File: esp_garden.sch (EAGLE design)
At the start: 40 parts, among them IC1 REG1117, T1 DMN6068SE-13, T2 DMN6068SE-13, T3 DMN6068SE-13, T4 DMN6068SE-13, U1 V1, U10 V1, U11 V1, U12 V1, U14 V1, U15 V1, U2 V1, U3 V1, U4 V1, U5 V1, U6 V1, U7 V1, U8 V1, U9 V1

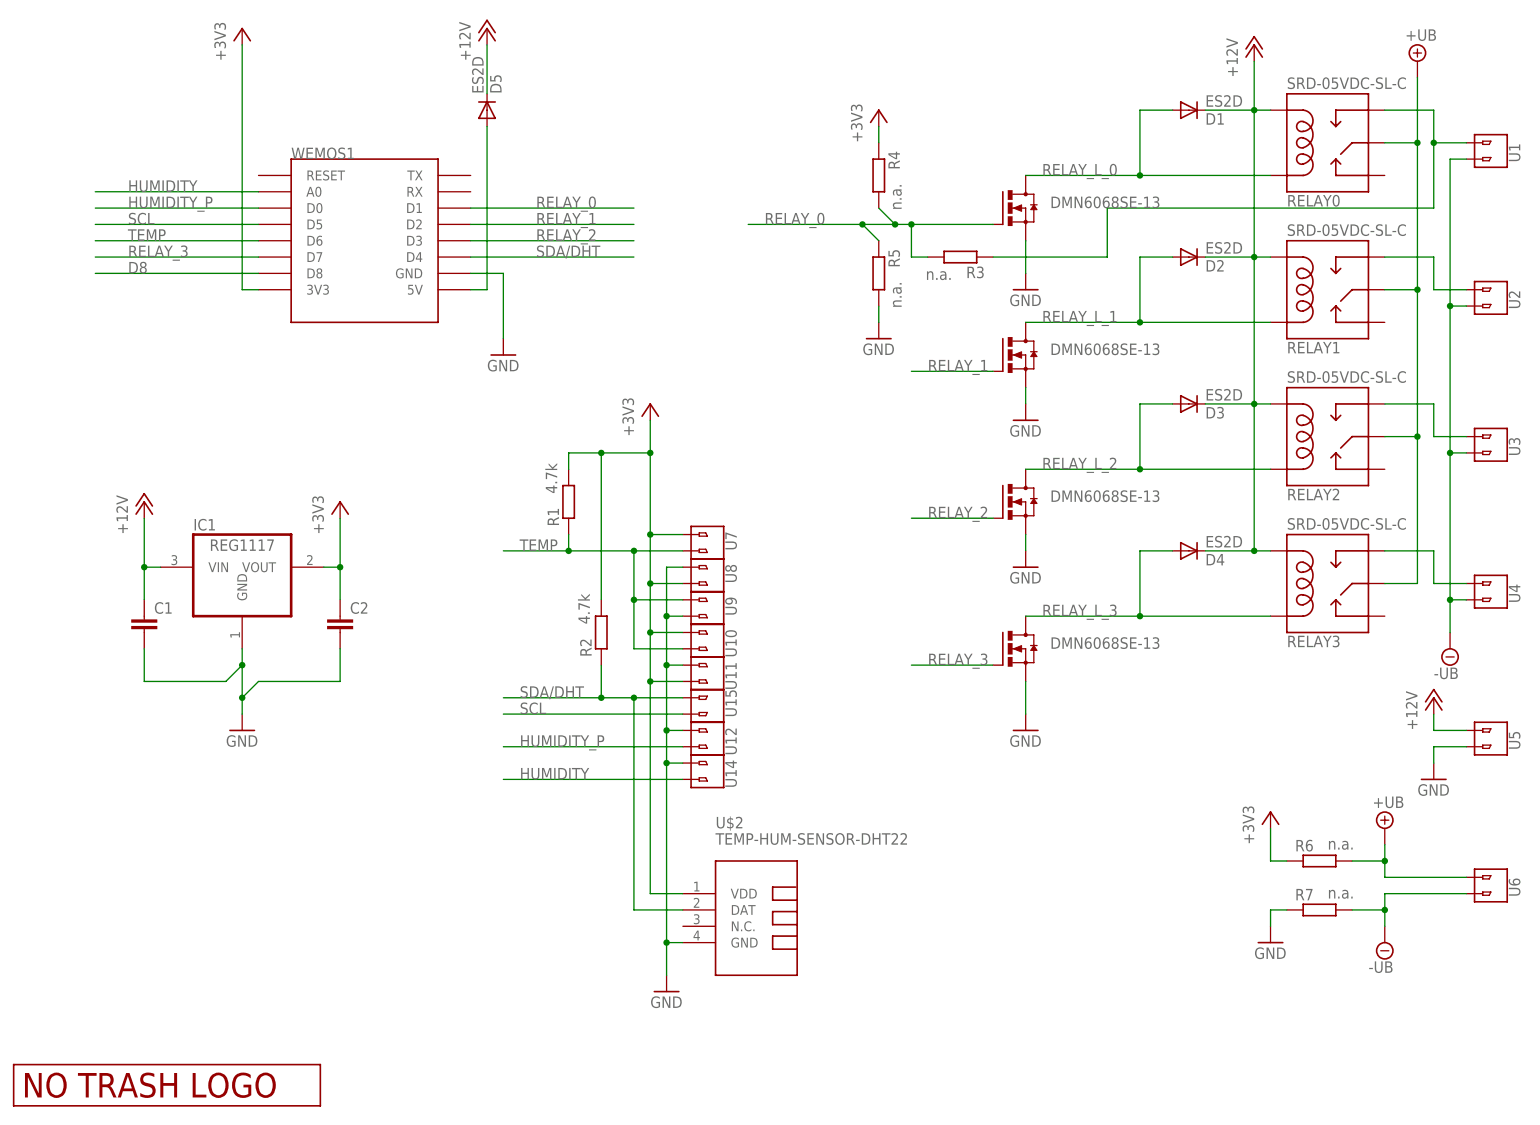
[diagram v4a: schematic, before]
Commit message: added rectifier
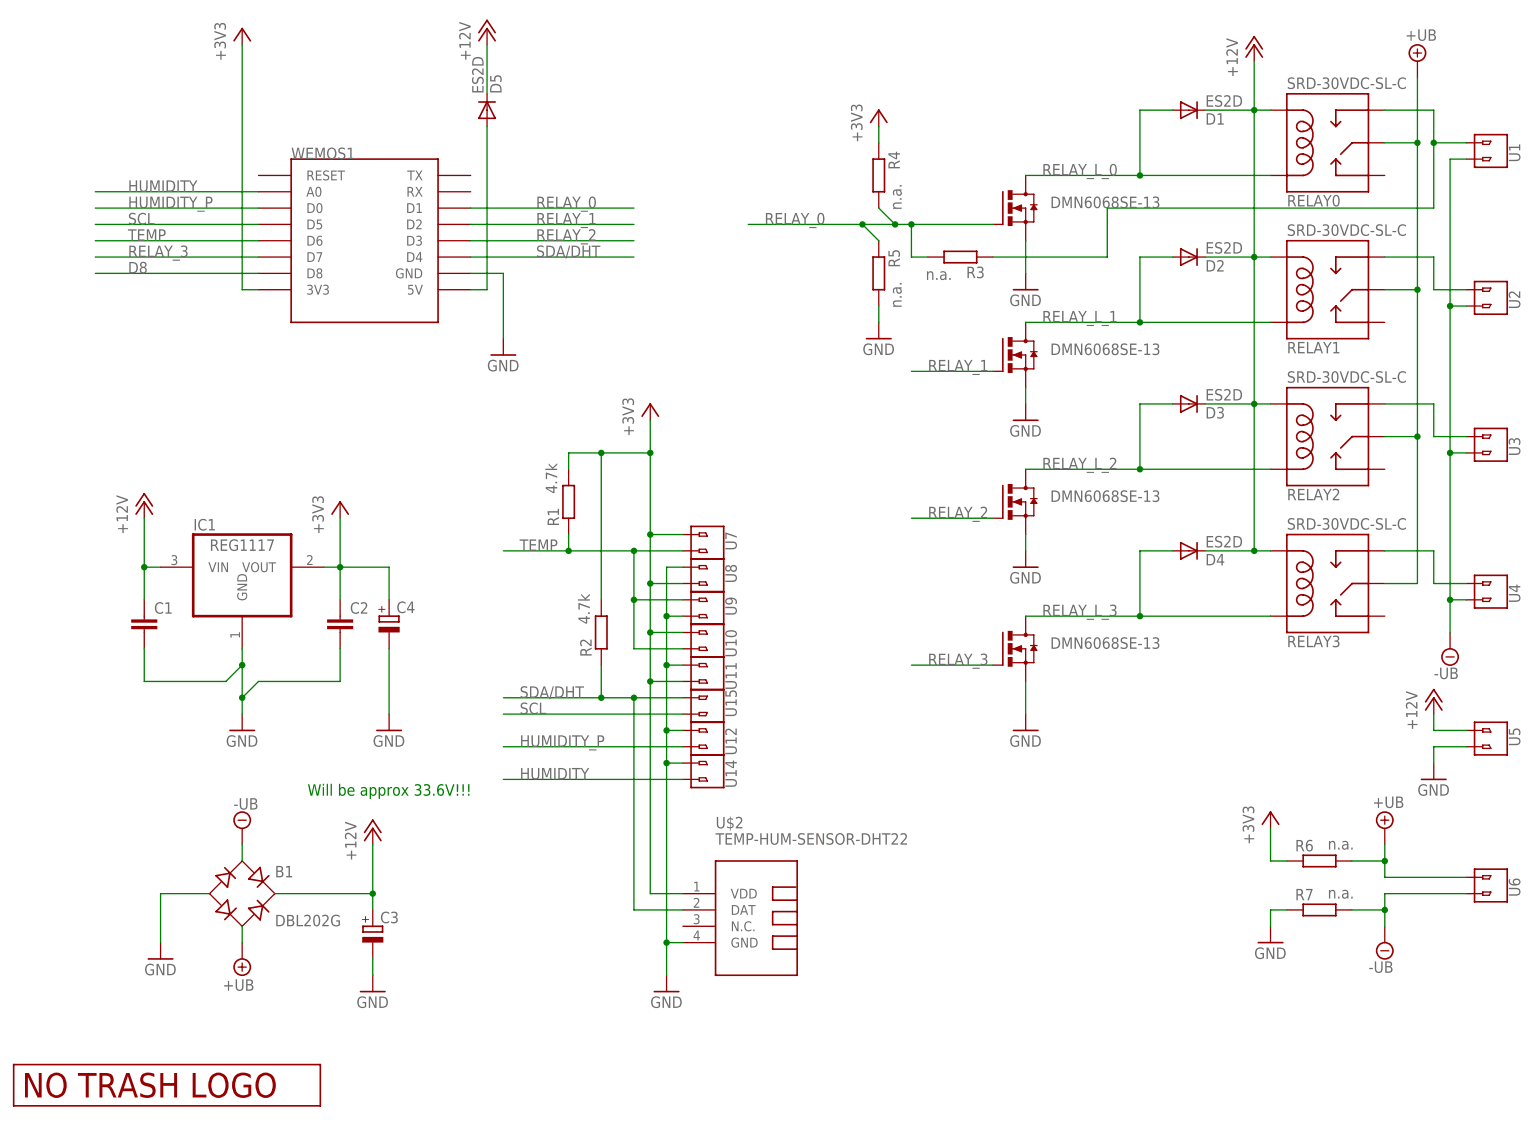
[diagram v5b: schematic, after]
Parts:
- added B1: DBL202G, rectifier:DBL202G
- added C3, C4: (no value), rcl:CPOL-EU150CLZ-0810
- RELAY0, RELAY1, RELAY2, RELAY3: value SRD-05VDC-SL-C -> SRD-30VDC-SL-C
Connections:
- net +12V: now also B1.+, C3.+, U5.2; no longer U5.1
- net +3V3: now also C4.+
- net +UB: now also B1.AC2
- net -UB: now also B1.AC1
- net GND: now also B1.-, C3.-, C4.-, U5.1; no longer U5.2
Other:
- note added: "Will be approx 33.6V!!!"
- moved on the sheet: U5
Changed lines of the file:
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@@
 <part name="FRAME1" library="frames" deviceset="A4L-LOC" device=""/>
 <part name="GND1" library="supply1" deviceset="GND" device=""/>
-<part name="RELAY0" library="JKW_CHIP" deviceset="RELAY" device="PTH" value="SRD-05VDC-SL-C"/>
+<part name="RELAY0" library="JKW_CHIP" deviceset="RELAY" device="PTH" value="SRD-30VDC-SL-C"/>
 <part name="T1" library="transistor-power" deviceset="NMOSFET_SMD_223" device="" value="DMN6068SE-13"/>
 <part name="GND8" library="supply1" deviceset="GND" device=""/>
@@
 <part name="GND7" library="supply1" deviceset="GND" device=""/>
 <part name="U2" library="JKW_CHIP" deviceset="2_PIN_CONNECTOR" device="" value="V1"/>
-<part name="RELAY1" library="JKW_CHIP" deviceset="RELAY" device="PTH" value="SRD-05VDC-SL-C"/>
+<part name="RELAY1" library="JKW_CHIP" deviceset="RELAY" device="PTH" value="SRD-30VDC-SL-C"/>
 <part name="T2" library="transistor-power" deviceset="NMOSFET_SMD_223" device="" value="DMN6068SE-13"/>
 <part name="GND3" library="supply1" deviceset="GND" device=""/>
 <part name="D2" library="diode" deviceset="DIODE-" device="SMB" value="ES2D"/>
-<part name="RELAY2" library="JKW_CHIP" deviceset="RELAY" device="PTH" value="SRD-05VDC-SL-C"/>
+<part name="RELAY2" library="JKW_CHIP" deviceset="RELAY" device="PTH" value="SRD-30VDC-SL-C"/>
 <part name="T3" library="transistor-power" deviceset="NMOSFET_SMD_223" device="" value="DMN6068SE-13"/>
 <part name="GND5" library="supply1" deviceset="GND" device=""/>
 <part name="D3" library="diode" deviceset="DIODE-" device="SMB" value="ES2D"/>
-<part name="RELAY3" library="JKW_CHIP" deviceset="RELAY" device="PTH" value="SRD-05VDC-SL-C"/>
+<part name="RELAY3" library="JKW_CHIP" deviceset="RELAY" device="PTH" value="SRD-30VDC-SL-C"/>
 <part name="T4" library="transistor-power" deviceset="NMOSFET_SMD_223" device="" value="DMN6068SE-13"/>
 <part name="GND10" library="supply1" deviceset="GND" device=""/>
@@
 <part name="GND9" library="supply1" deviceset="GND" device=""/>
 <part name="+3V5" library="supply1" deviceset="+3V3" device=""/>
+<part name="B1" library="rectifier" deviceset="DB?*G" device="L20" technology="2"/>
+<part name="SUPPLY5" library="supply2" deviceset="+UB" device=""/>
+<part name="SUPPLY6" library="supply2" deviceset="-UB" device=""/>
+<part name="P+4" library="supply1" deviceset="+12V" device=""/>
+<part name="GND11" library="supply1" deviceset="GND" device=""/>
+<part name="C3" library="rcl" deviceset="CPOL-EU" device="150CLZ-0810"/>
+<part name="C4" library="rcl" deviceset="CPOL-EU" device="150CLZ-0810"/>
+<part name="GND12" library="supply1" deviceset="GND" device=""/>
+<part name="GND13" library="supply1" deviceset="GND" device=""/>
 </parts>
 <sheets>
 <sheet>
 <plain>
+<text x="20.32" y="50.8" size="1.778" layer="91">Will be approx 33.6V!!!</text>
 </plain>
 <instances>
@@
 <attribute name="NAME" x="209.042" y="103.632" size="1.778" layer="95" rot="R90"/>
 </instance>
-<instance part="U5" gate="G$1" x="200.66" y="58.42" smashed="yes">
-<attribute name="NAME" x="209.042" y="57.912" size="1.778" layer="95" rot="R90"/>
+<instance part="U5" gate="G$1" x="200.66" y="60.96" smashed="yes" rot="MR180">
+<attribute name="NAME" x="209.042" y="61.468" size="1.778" layer="95" rot="MR270"/>
 </instance>
 <instance part="GND4" gate="1" x="10.16" y="60.96"/>
@@
 <instance part="GND9" gate="1" x="170.18" y="27.94"/>
 <instance part="+3V5" gate="G$1" x="170.18" y="48.26"/>
+<instance part="B1" gate="G$1" x="10.16" y="35.56"/>
+<instance part="SUPPLY5" gate="G$1" x="10.16" y="25.4" rot="R180"/>
+<instance part="SUPPLY6" gate="G$1" x="10.16" y="45.72" rot="R180"/>
+<instance part="P+4" gate="1" x="30.48" y="45.72"/>
+<instance part="GND11" gate="1" x="-2.54" y="25.4"/>
+<instance part="C3" gate="G$1" x="30.48" y="30.48"/>
+<instance part="C4" gate="G$1" x="33.02" y="78.74"/>
+<instance part="GND12" gate="1" x="33.02" y="60.96"/>
+<instance part="GND13" gate="1" x="30.48" y="20.32"/>
 </instances>
 <busses>
@@
 </segment>
 <segment>
-<pinref part="U5" gate="G$1" pin="2"/>
 <pinref part="GND6" gate="1" pin="GND"/>
-<wire x1="200.66" y1="58.42" x2="195.58" y2="58.42" width="0.1524" layer="91"/>
 <wire x1="195.58" y1="58.42" x2="195.58" y2="55.88" width="0.1524" layer="91"/>
+<pinref part="U5" gate="G$1" pin="1"/>
+<wire x1="195.58" y1="58.42" x2="200.66" y2="58.42" width="0.1524" layer="91"/>
 </segment>
 <segment>
@@
 <pinref part="GND2" gate="1" pin="GND"/>
 <wire x1="109.22" y1="124.46" x2="109.22" y2="127" width="0.1524" layer="91"/>
+</segment>
+<segment>
+<pinref part="B1" gate="G$1" pin="-"/>
+<pinref part="GND11" gate="1" pin="GND"/>
+<wire x1="5.08" y1="35.56" x2="-2.54" y2="35.56" width="0.1524" layer="91"/>
+<wire x1="-2.54" y1="35.56" x2="-2.54" y2="27.94" width="0.1524" layer="91"/>
+</segment>
+<segment>
+<pinref part="GND13" gate="1" pin="GND"/>
+<pinref part="C3" gate="G$1" pin="-"/>
+<wire x1="30.48" y1="22.86" x2="30.48" y2="25.4" width="0.1524" layer="91"/>
+</segment>
+<segment>
+<pinref part="GND12" gate="1" pin="GND"/>
+<pinref part="C4" gate="G$1" pin="-"/>
+<wire x1="33.02" y1="63.5" x2="33.02" y2="73.66" width="0.1524" layer="91"/>
 </segment>
 </net>
@@
 </segment>
 <segment>
-<pinref part="U5" gate="G$1" pin="1"/>
 <pinref part="P+1" gate="1" pin="+12V"/>
-<wire x1="200.66" y1="60.96" x2="195.58" y2="60.96" width="0.1524" layer="91"/>
 <wire x1="195.58" y1="60.96" x2="195.58" y2="63.5" width="0.1524" layer="91"/>
+<pinref part="U5" gate="G$1" pin="2"/>
+<wire x1="195.58" y1="60.96" x2="200.66" y2="60.96" width="0.1524" layer="91"/>
 </segment>
 <segment>
@@
 <wire x1="-2.54" y1="86.36" x2="-5.08" y2="86.36" width="0.1524" layer="91"/>
 <junction x="-5.08" y="86.36"/>
+</segment>
+<segment>
+<pinref part="B1" gate="G$1" pin="+"/>
+<pinref part="P+4" gate="1" pin="+12V"/>
+<wire x1="15.24" y1="35.56" x2="30.48" y2="35.56" width="0.1524" layer="91"/>
+<wire x1="30.48" y1="35.56" x2="30.48" y2="43.18" width="0.1524" layer="91"/>
+<pinref part="C3" gate="G$1" pin="+"/>
+<wire x1="30.48" y1="33.02" x2="30.48" y2="35.56" width="0.1524" layer="91"/>
+<junction x="30.48" y="35.56"/>
 </segment>
 </net>
@@
 <wire x1="22.86" y1="86.36" x2="25.4" y2="86.36" width="0.1524" layer="91"/>
 <junction x="25.4" y="86.36"/>
+<pinref part="C4" gate="G$1" pin="+"/>
+<wire x1="25.4" y1="86.36" x2="33.02" y2="86.36" width="0.1524" layer="91"/>
+<wire x1="33.02" y1="86.36" x2="33.02" y2="81.28" width="0.1524" layer="91"/>
 </segment>
 <segment>
@@
 <junction x="193.04" y="106.68"/>
 </segment>
+<segment>
+<pinref part="SUPPLY5" gate="G$1" pin="+UB"/>
+<pinref part="B1" gate="G$1" pin="AC2"/>
+<wire x1="10.16" y1="27.94" x2="10.16" y2="30.48" width="0.1524" layer="91"/>
+</segment>
 </net>
 <net name="-UB" class="0">
@@
 <junction x="198.12" y="81.28"/>
 </segment>
-</net>
+<segment>
+<pinref part="B1" gate="G$1" pin="AC1"/>
+<pinref part="SUPPLY6" gate="G$1" pin="-UB"/>
+<wire x1="10.16" y1="40.64" x2="10.16" y2="43.18" width="0.1524" layer="91"/>
+</segment>
+</net>
